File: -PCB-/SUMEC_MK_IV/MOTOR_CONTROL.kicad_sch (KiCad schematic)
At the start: 20 parts, among them IC2 DRV8874PWPR, IC3 DRV8874PWPR

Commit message: v3.0.9 SUMEC PCB
Ufff, so, basically a full rewrite of the PCB, check it our its pretty sick, I think
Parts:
- removed R13, R14, R15, R16: 0R, Resistor_SMD:R_0805_2012Metric_Pad1.20x1.40mm_HandSolder, symbol Device:R
- renumbered C13 to C11, C14 to C12, C15 to C13, C16 to C14, C17 to C15, C18 to C16, C19 to C17, C20 to C18, R12 to R10, R7 to R5, R8 to R6, R9 to R7, R10 to R8, R11 to R9
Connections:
- net GND: now also IC2.16 (PMODE), IC3.16 (PMODE)
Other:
- note added: "THERE WERE 2 OR RESISTORS, ONE FOR VCC THE OTHER IS FOR GND, PURPOSE: CHOICE BETWEEEN GND AND VCC FOR TWO MODES"

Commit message: minor updates
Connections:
- net IPROPI_ADC: no longer names the net of IC2.6 (IPROPI), R5.2
- net IPROPI_ADC: no longer IC3.6 (IPROPI), R7.2
- new net: IC3.6 (IPROPI), R7.2
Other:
- moved on the sheet: R5, R6, R7, R8

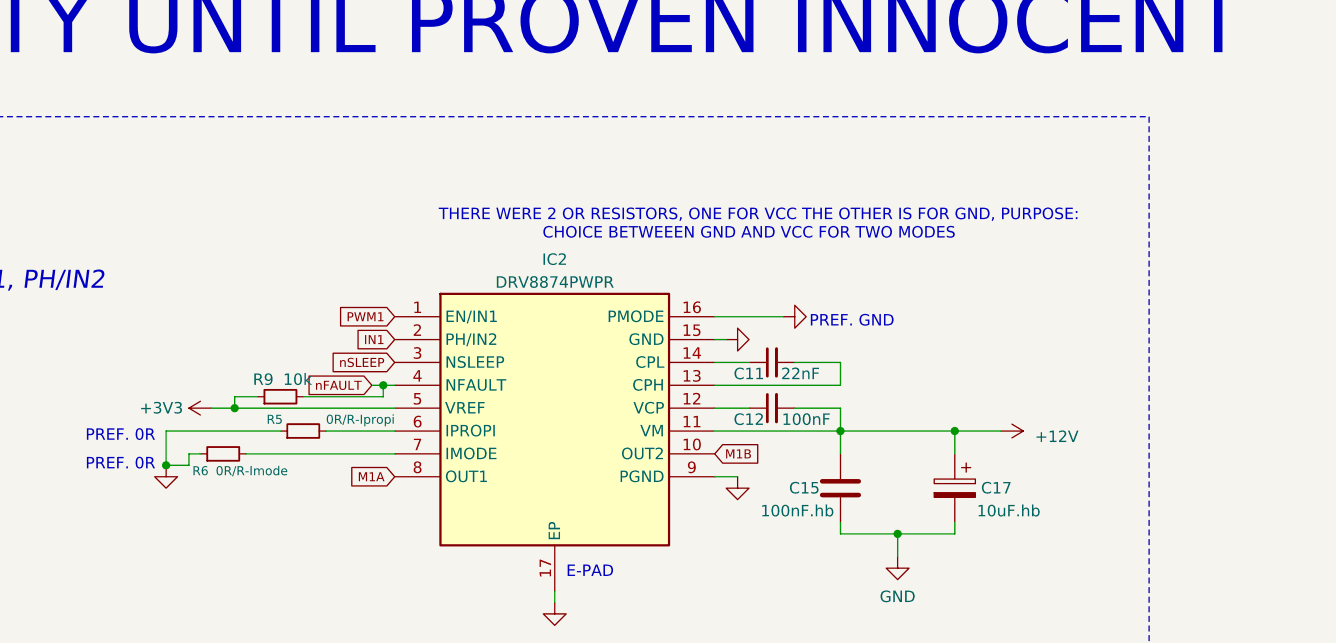
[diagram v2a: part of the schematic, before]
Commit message: Trace distance minor change
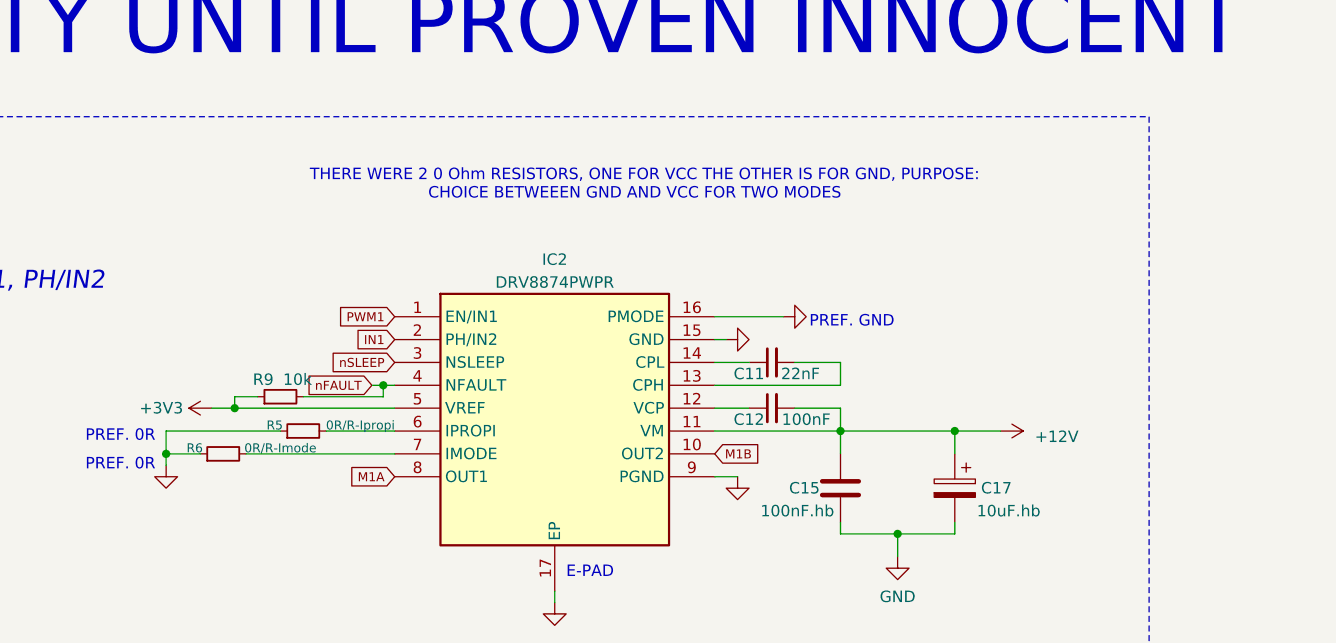
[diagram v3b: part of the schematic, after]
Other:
- note added: "THERE WERE 2 0 Ohm RESISTORS, ONE FOR VCC THE OTHER IS FOR GND, PURPOSE: CHOICE BETWEEEN GND AND VCC FOR TWO MODES"
- note removed: "THERE WERE 2 OR RESISTORS, ONE FOR VCC THE OTHER IS FOR GND, PURPOSE: CHOICE BETWEEEN GND AND VCC FOR TWO MODES"
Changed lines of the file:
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@@
 	)
 	(junction
-		(at 130.81 74.93)
-		(diameter 0)
-		(color 0 0 0 0)
-	)
-	(junction
 		(at 218.44 71.12)
 		(diameter 0)
@@
 		(color 0 0 0 0)
 	)
+	(junction
+		(at 130.81 73.66)
+		(diameter 0)
+		(color 0 0 0 0)
+	)
 	(wire
 		(pts
@@
 	(wire
 		(pts
-			(xy 133.35 74.93) (xy 130.81 74.93)
+			(xy 130.81 73.66) (xy 134.62 73.66)
 		)
 		(stroke
@@
 	(wire
 		(pts
-			(xy 133.35 73.66) (xy 134.62 73.66)
+			(xy 218.44 82.55) (xy 218.44 81.28)
 		)
 		(stroke
@@
 	(wire
 		(pts
-			(xy 218.44 82.55) (xy 218.44 81.28)
+			(xy 173.99 90.17) (xy 173.99 88.9)
 		)
 		(stroke
@@
 	(wire
 		(pts
-			(xy 173.99 90.17) (xy 173.99 88.9)
+			(xy 200.66 118.11) (xy 205.74 118.11)
 		)
 		(stroke
@@
 	(wire
 		(pts
-			(xy 200.66 118.11) (xy 205.74 118.11)
+			(xy 205.74 71.12) (xy 218.44 71.12)
 		)
 		(stroke
@@
 	(wire
 		(pts
-			(xy 205.74 71.12) (xy 218.44 71.12)
+			(xy 191.77 118.11) (xy 195.58 118.11)
 		)
 		(stroke
@@
 	(wire
 		(pts
-			(xy 191.77 118.11) (xy 195.58 118.11)
+			(xy 130.81 71.12) (xy 130.81 73.66)
 		)
 		(stroke
@@
 	(wire
 		(pts
-			(xy 130.81 71.12) (xy 130.81 74.93)
+			(xy 130.81 73.66) (xy 130.81 74.93)
 		)
 		(stroke
@@
 	(wire
 		(pts
-			(xy 133.35 73.66) (xy 133.35 74.93)
-		)
-		(stroke
-			(width 0)
-			(type default)
-		)
-	)
-	(wire
-		(pts
 			(xy 205.74 82.55) (xy 205.74 81.28)
 		)
@@
 		)
 	)
-	(text "	THERE WERE 2 OR RESISTORS, ONE FOR VCC THE OTHER IS FOR GND, PURPOSE: \nCHOICE BETWEEEN GND AND VCC FOR TWO MODES"
+	(text "	THERE WERE 2 0 Ohm RESISTORS, ONE FOR VCC THE OTHER IS FOR GND, PURPOSE: \nCHOICE BETWEEEN GND AND VCC FOR TWO MODES"
 		(exclude_from_sim no)
-		(at 195.58 48.26 0)
+		(at 182.88 43.815 0)
 		(effects
 			(font
@@
 		(dnp no)
 		(property "Reference" "R6"
-			(at 134.62 75.565 90)
+			(at 133.985 73.025 90)
 			(effects
 				(font
@@
 		)
 		(property "Value" "0R/R-Imode"
-			(at 140.335 75.565 90)
+			(at 143.51 73.025 90)
 			(effects
 				(font
@@
 		(dnp no)
 		(property "Reference" "R5"
-			(at 142.875 69.85 90)
+			(at 142.875 70.485 90)
 			(effects
 				(font
@@
 		)
 		(property "Value" "0R/R-Ipropi"
-			(at 152.4 69.85 90)
+			(at 152.4 70.485 90)
 			(effects
 				(font

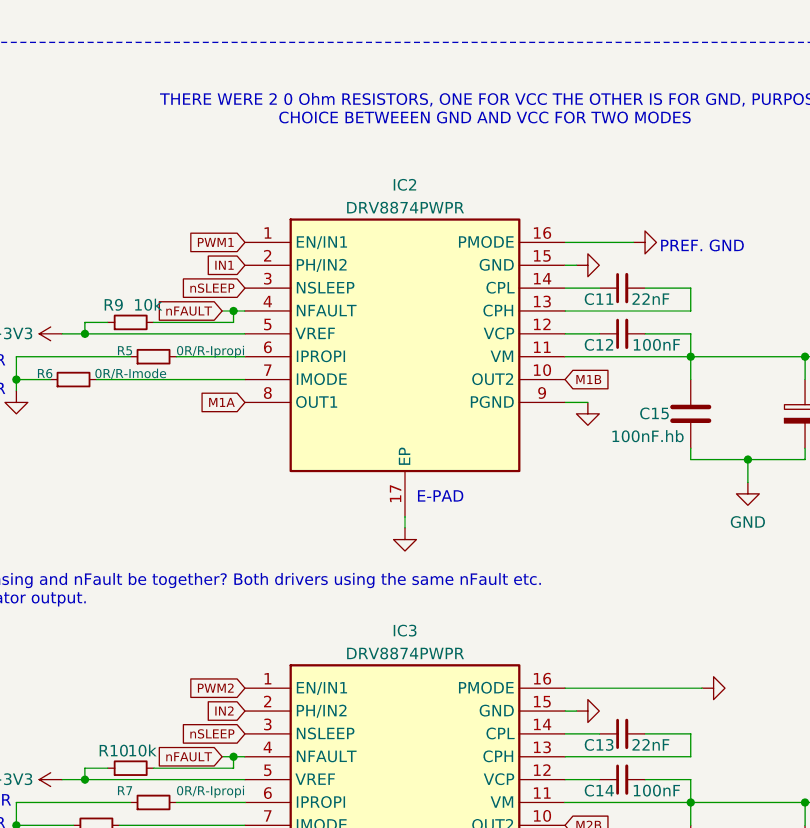
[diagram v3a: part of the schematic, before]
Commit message: Dimensions back and front, 3d models for footprints.
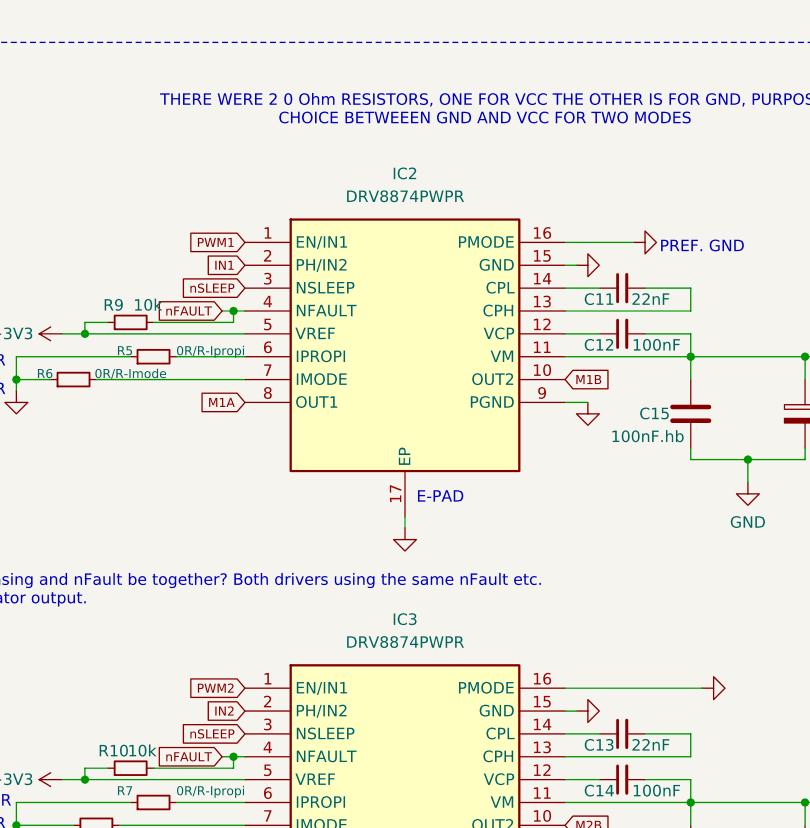
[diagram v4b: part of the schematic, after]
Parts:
- removed IC2, IC3: DRV8874PWPR, sumec-smdV2_library:DRV8874, symbol sumec_library:DRV8874PWPR
- added IC2, IC3: DRV8874PWPR, sumec_brd:DRV8874, symbol sumec_sch_lib:DRV8874PWPR
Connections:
- net +12V: now also IC2.11 (VM), IC3.11 (VM)
- net +3V3: now also IC2.5 (VREF), IC3.5 (VREF)
- net GND: now also IC2.15 (GND), IC2.16 (PMODE), IC2.17 (EP), IC2.9 (PGND), IC3.15 (GND), IC3.16 (PMODE), IC3.17 (EP), IC3.9 (PGND)
- net IN1: now also IC2.2 (PH/IN2)
- net IN2: now also IC3.2 (PH/IN2)
- net M1A: now also IC2.8 (OUT1)
- net M1B: now also IC2.10 (OUT2)
- net M2A: now also IC3.8 (OUT1)
- net M2B: now also IC3.10 (OUT2)
- net PWM1: now also IC2.1 (EN/IN1)
- net PWM2: now also IC3.1 (EN/IN1)
- net nFAULT: now also IC2.4 (NFAULT), IC3.4 (NFAULT)
- net nSLEEP: now also IC2.3 (NSLEEP), IC3.3 (NSLEEP)
- net at C14.1: now also IC3.12 (VCP)
- net at C11.1: now also IC2.14 (CPL)
- net at C11.2: now also IC2.13 (CPH)
- net at R6.2: now also IC2.7 (IMODE)
- net at C12.1: now also IC2.12 (VCP)
- net at R5.2: now also IC2.6 (IPROPI)
- net at C13.1: now also IC3.14 (CPL)
- net at C13.2: now also IC3.13 (CPH)
- net at R8.2: now also IC3.7 (IMODE)
- net at R7.2: now also IC3.6 (IPROPI)

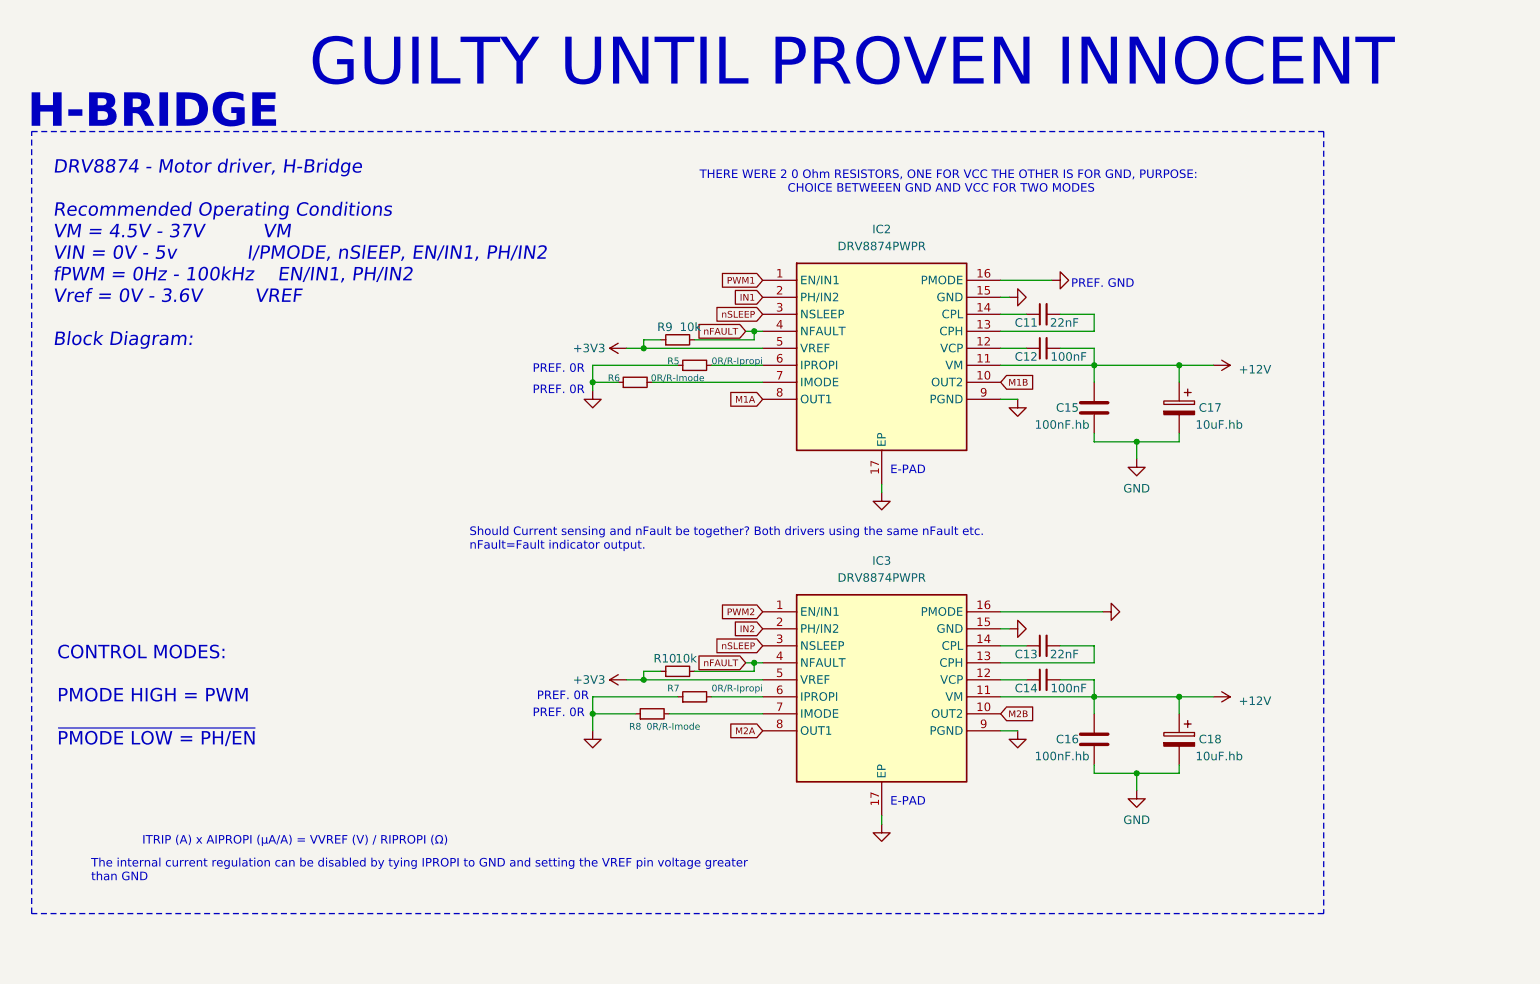
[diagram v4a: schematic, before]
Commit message: Schematic and PCB update
Schematic update:
- Font adjustment
- Block rearrangement

PCB update
- Silkscreen
- Minor layout update
- Graphic update
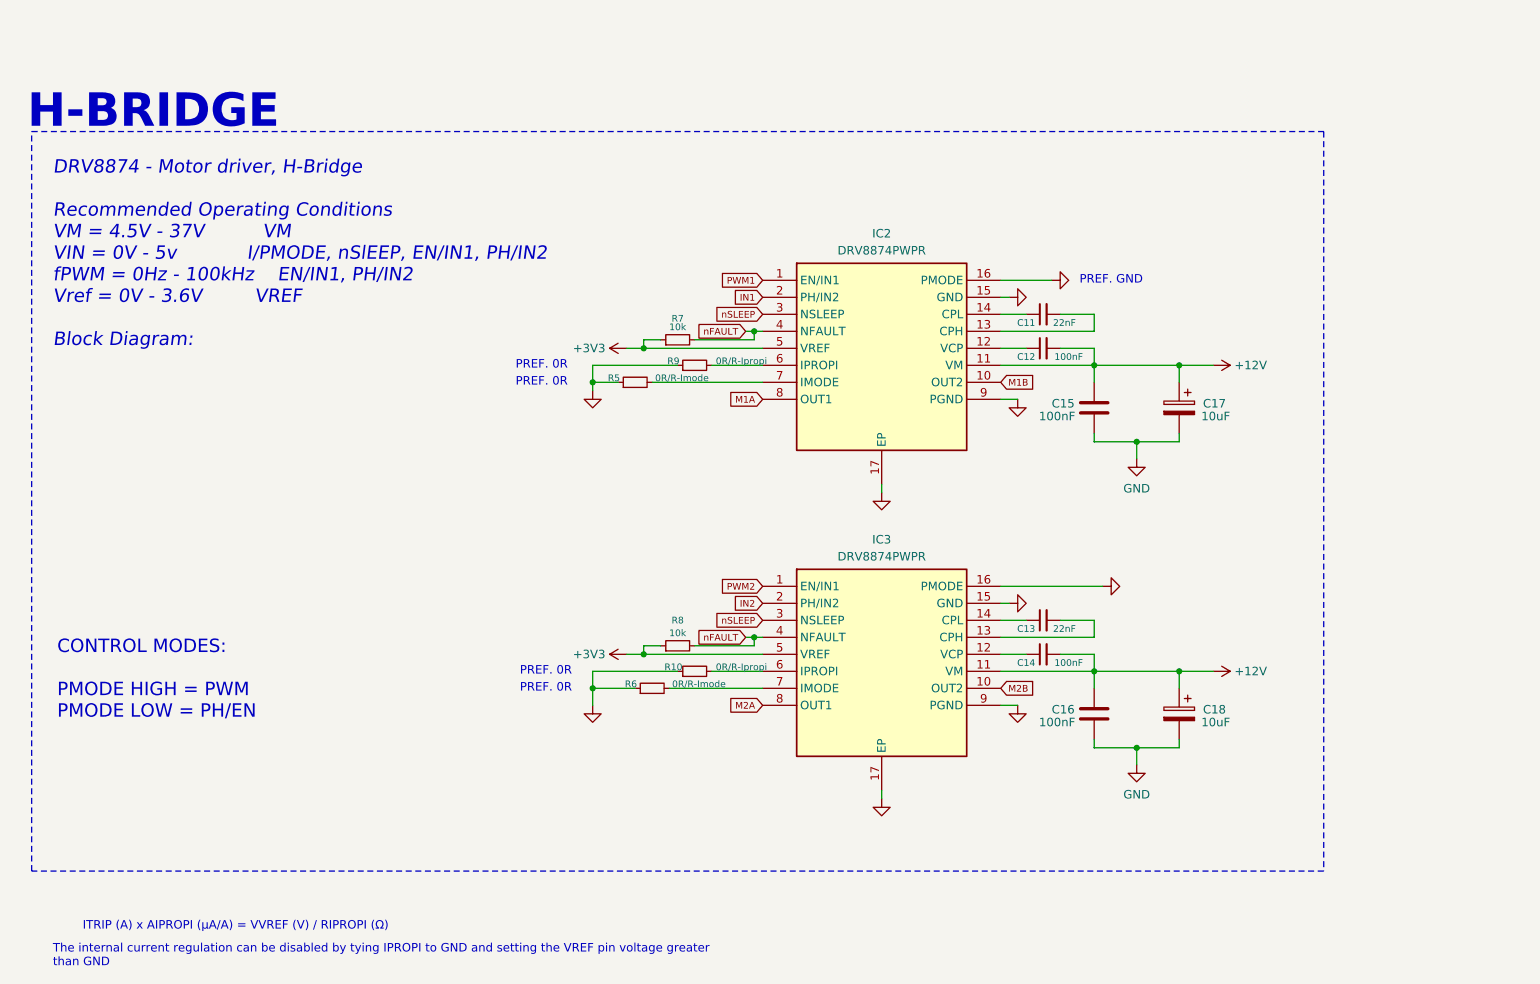
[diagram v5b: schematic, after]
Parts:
- C15, C16: value 100nF.hb -> 100nF
- C17, C18: value 10uF.hb -> 10uF
- renumbered R7 to R10, R6 to R5, R8 to R6, R9 to R7, R10 to R8, R5 to R9
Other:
- note added: "CONTROL MODES: PMODE HIGH = PWM PMODE LOW = PH/EN"
- note removed: "CONTROL MODES: PMODE HIGH = PWM ~{PMODE LOW = PH/EN}"
- note removed: "E-PAD"
- note removed: "GUILTY UNTIL PROVEN INNOCENT"
- note removed: "Should Current sensing and nFault be together? Both drivers using the same nFault etc. nFault=Fault indicator output."
- note removed: "THERE WERE 2 0 Ohm RESISTORS, ONE FOR VCC THE OTHER IS FOR GND, PURPOSE: CHOICE BETWEEEN GND AND VCC FOR TWO MODES"
- moved on the sheet: C13, C14, C16, C18, IC3, R10, R6, R8

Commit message: 3d filepath fix, long filepath fix
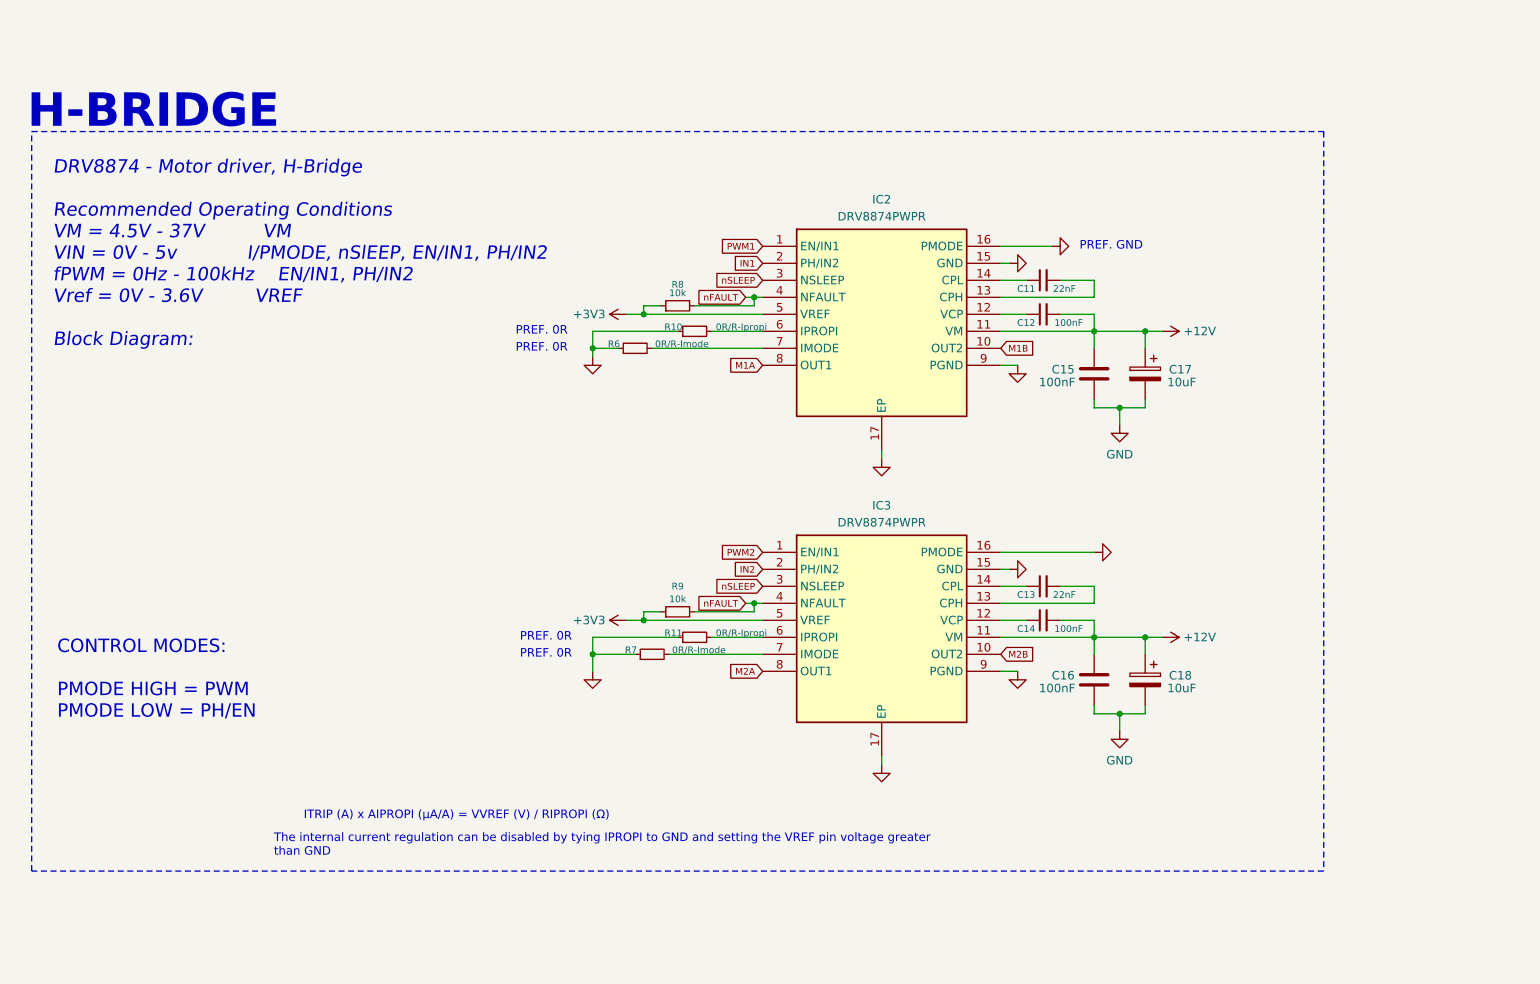
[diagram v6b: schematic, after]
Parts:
- renumbered R9 to R10, R10 to R11, R5 to R6, R6 to R7, R7 to R8, R8 to R9
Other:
- moved on the sheet: C11, C12, C13, C14, C15, C16, C17, C18, IC2, IC3, R10, R11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
